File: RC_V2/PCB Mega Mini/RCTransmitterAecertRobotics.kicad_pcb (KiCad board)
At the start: 2 copper layers, 124.5 x 86.4 mm, 39 parts, among them K1 KCD1 Power Switch

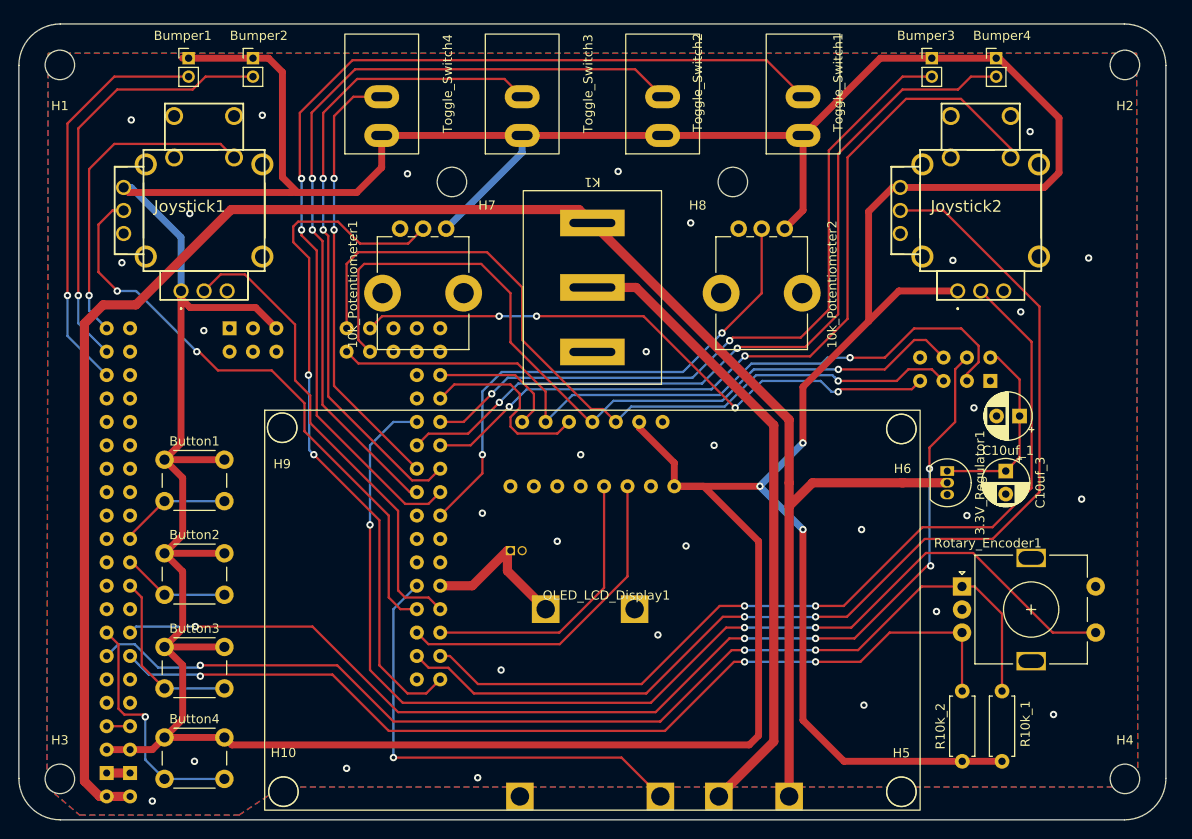
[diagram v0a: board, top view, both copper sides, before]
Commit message: rcv2 pcb finished, added new gait
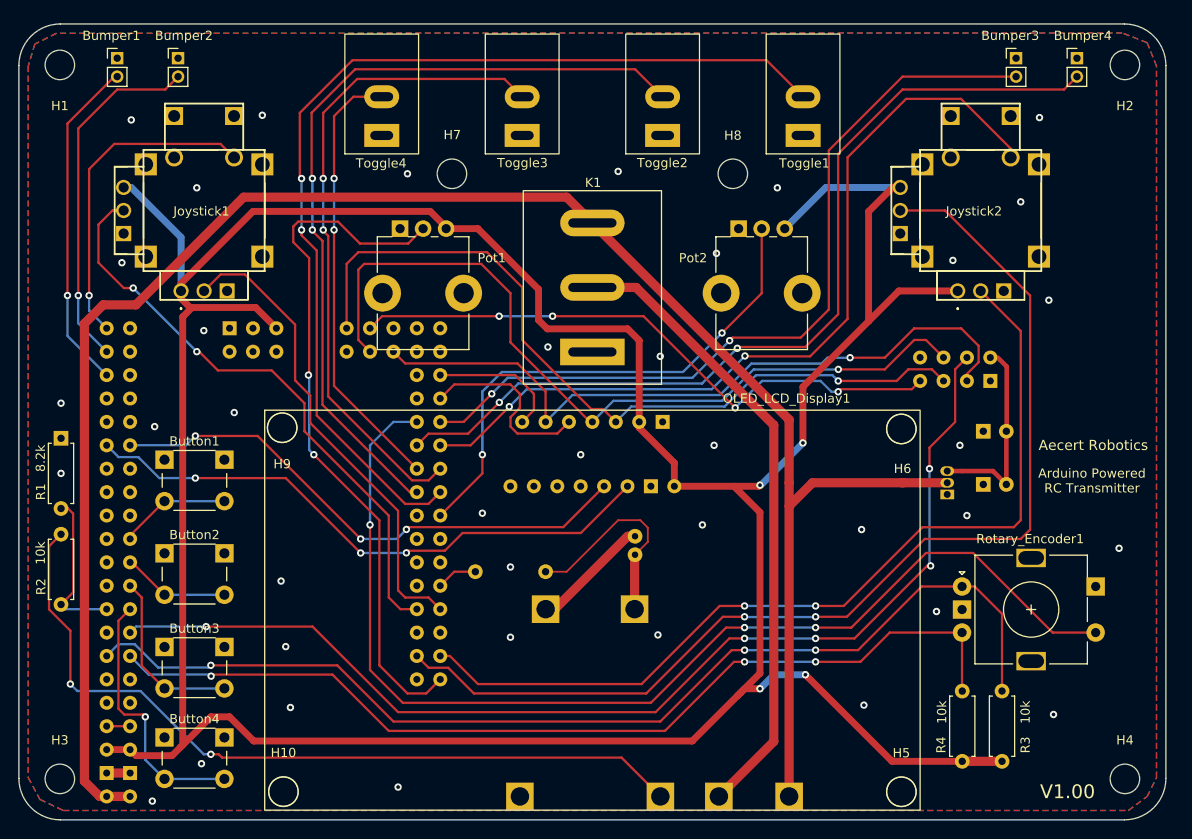
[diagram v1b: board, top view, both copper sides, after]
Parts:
- added G***: LOGO, LOGO, F.Cu at (195.8, 91.4)
- added R1: 8.2k, Resistor_THT:R_Axial_DIN0207_L6.3mm_D2.5mm_P7.62mm_Horizontal, F.Cu at (83.3, 100.8)
- added R2: 10k, Resistor_THT:R_Axial_DIN0207_L6.3mm_D2.5mm_P7.62mm_Horizontal, F.Cu at (83.3, 118.9)
- added R5: 10k, Resistor_THT:R_Axial_DIN0207_L6.3mm_D2.5mm_P7.62mm_Horizontal, B.Cu at (135.9, 115.3)
- 3.3V_Reg1: renamed from 3.3V_Regulator1; moved to B.Cu
- Arduino_Mega_Pro1: renamed from M1; value ~ -> Arduino Mega Pro Mini
- C1: renamed from C10uf_1; moved to B.Cu
- C2: renamed from C10uf_3; moved to B.Cu
- JST_Connector1: footprint Connector_PinSocket_1.27mm:PinSocket_1x02_P1.27mm_Vertical -> AddedFootprints:JST Female Connector
- Pot1: renamed from 10k_Potentiometer1; value PTV09A-4220F-B103 -> 10k
- Pot2: renamed from 10k_Potentiometer2; value PTV09A-4220F-B103 -> 10k
- R3: renamed from R10k_1; value R 10k -> 10k
- R4: renamed from R10k_2; value R 10k -> 10k
- moved JST_Connector1 14.8 mm to (145.6, 107.1), turned to 0 degrees
- moved Bumper3 9.14 mm to (186.9, 59.6)
- moved Bumper4 8.76 mm to (193.5, 59.6)
- moved Bumper2 8.13 mm to (96.0, 59.6)
- moved Bumper1 7.75 mm to (89.4, 59.6)
- moved C1 2.19 mm to (185.9, 100.1)
- moved C2 1.45 mm to (185.9, 105.8), turned to 180 degrees
- moved H7 0.89 mm to (125.7, 72.1)
- moved H8 0.89 mm to (156.2, 72.1)
- renumbered Toggle_Switch1 to Toggle1, Toggle_Switch2 to Toggle2, Toggle_Switch3 to Toggle3, Toggle_Switch4 to Toggle4
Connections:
- Arduino_Mega_Pro1 pad 20: unconnected-(M1-D20(SDA)-Pad20) -> /SDA
- Arduino_Mega_Pro1 pad 21: unconnected-(M1-D21(SCL)-Pad21) -> /SCL
- Arduino_Mega_Pro1 pad 49: unconnected-(M1-D49-Pad49) -> /CE
- Arduino_Mega_Pro1 pad 5: /Button D -> unconnected-(Arduino_Mega_Pro1-D5-Pad5)
- Arduino_Mega_Pro1 pad 53: /CE -> unconnected-(Arduino_Mega_Pro1-D53(CE)-Pad53)
- Arduino_Mega_Pro1 pad 6: unconnected-(M1-D6-Pad6) -> /Button D
- Arduino_Mega_Pro1 pad 7: unconnected-(M1-D7-Pad7) -> /Charging
- Arduino_Mega_Pro1 pad A4: /SDA -> unconnected-(Arduino_Mega_Pro1-PadA4)
- Arduino_Mega_Pro1 pad A5: /SCL -> unconnected-(Arduino_Mega_Pro1-PadA5)
- Arduino_Mega_Pro1 pad A8: /Bat+ -> /Battery Voltage
- Arduino_Mega_Pro1 pad A9: /In+ -> unconnected-(Arduino_Mega_Pro1-PadA9)
- Battery_Charger1 pad 3: /In+ -> Net-(Battery_Charger1-IN+)
- Bumper1 pad 1: /5v -> GND
- Bumper2 pad 1: /5v -> GND
- Bumper3 pad 1: /5v -> GND
- Bumper4 pad 1: /5v -> GND
- Button1 pad 1: /5v -> GND
- Button2 pad 1: /5v -> GND
- Button3 pad 1: /5v -> GND
- Button4 pad 1: /5v -> GND
- Joystick1 pad D1: unconnected-(Joystick1-NO_2-PadD1) -> GND
- Joystick1 pad MH1: unconnected-(Joystick1-PadMH1) -> GND
- Joystick1 pad MH2: unconnected-(Joystick1-PadMH2) -> GND
- Joystick1 pad MH3: unconnected-(Joystick1-PadMH3) -> GND
- Joystick1 pad MH4: unconnected-(Joystick1-PadMH4) -> GND
- Joystick2 pad D1: unconnected-(Joystick2-NO_2-PadD1) -> GND
- Joystick2 pad MH1: unconnected-(Joystick2-PadMH1) -> GND
- Joystick2 pad MH2: unconnected-(Joystick2-PadMH2) -> GND
- Joystick2 pad MH3: unconnected-(Joystick2-PadMH3) -> GND
- Joystick2 pad MH4: unconnected-(Joystick2-PadMH4) -> GND
- Toggle1 pad 1: /5v -> GND
- Toggle2 pad 1: /5v -> GND
- Toggle3 pad 1: /5v -> GND
- Toggle4 pad 1: /5v -> GND
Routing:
- net /5v: track 510.3 -> 361.0 mm, vias 3 -> 4
- net Net-(Battery_Charger1-IN+): track 0.00 -> 86.8 mm, vias 0 -> 2
- net /In+: track 50.4 -> 0.00 mm, vias 1 -> 0
- net /SCL: track 36.2 -> 64.4 mm, vias 0 -> 3
- net /SDA: track 30.8 -> 58.9 mm, vias 0 -> 3
- net /Charging: track 0.00 -> 17.1 mm
- net /Bat-: track 0.00 -> 13.0 mm
- net /Right Bumper A: track 79.0 -> 88.1 mm
- net /Right Bumper B: track 89.6 -> 98.4 mm
- net /Left Bumper B: track 46.8 -> 38.7 mm
- net /Left Bumper A: track 44.3 -> 36.6 mm
- net /Bat+: track 16.9 -> 23.2 mm
- net /CE: track 83.0 -> 77.9 mm
- net /Battery Voltage: track 0.00 -> 4.44 mm
- net /Button D: track 26.2 -> 28.7 mm
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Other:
- board text added: "+"
- board text added: "-"
- board text added: "Aecert Robotics"
- board text added: "Arduino Powered RC Transmitter"
- board text added: "V1.00"

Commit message: Fixed pin placement and hole diameter
after testing in real life, i made some changes
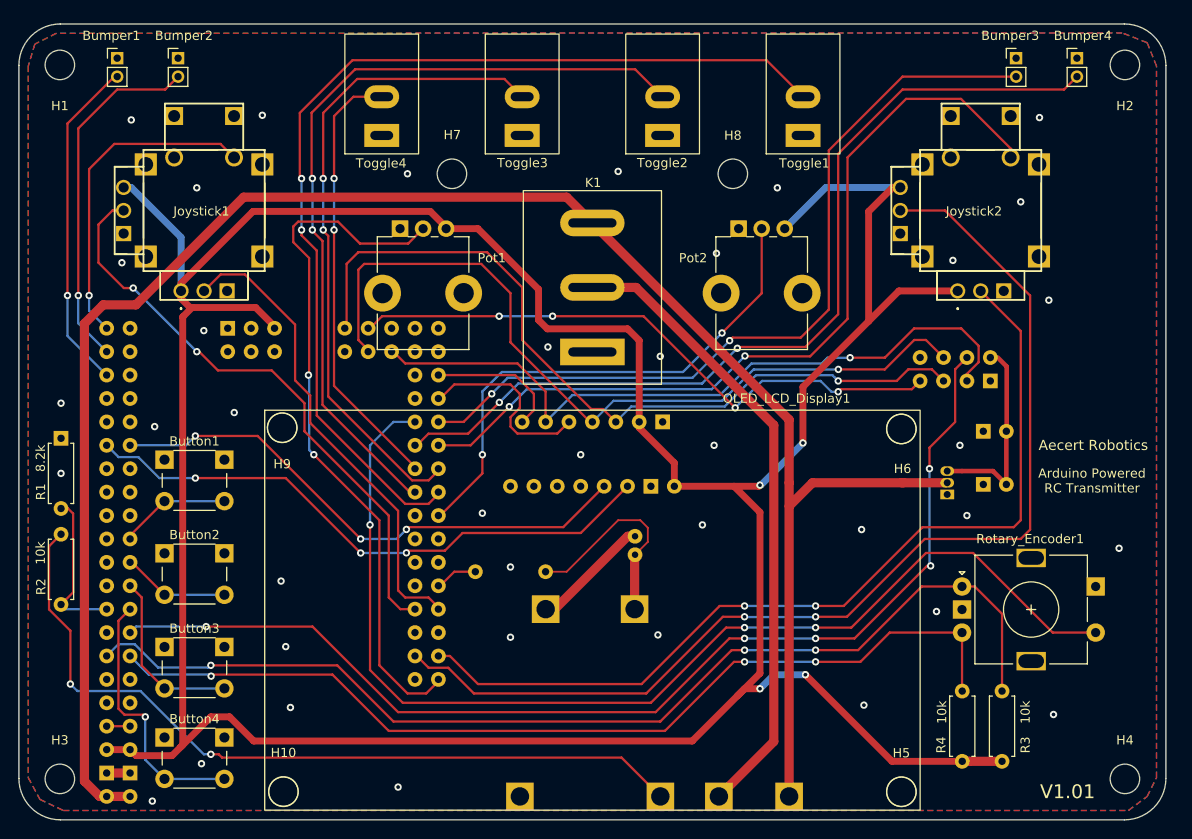
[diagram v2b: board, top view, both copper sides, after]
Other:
- board text added: "V1.01"
- board text removed: "V1.00"

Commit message: updated code pins and pcb
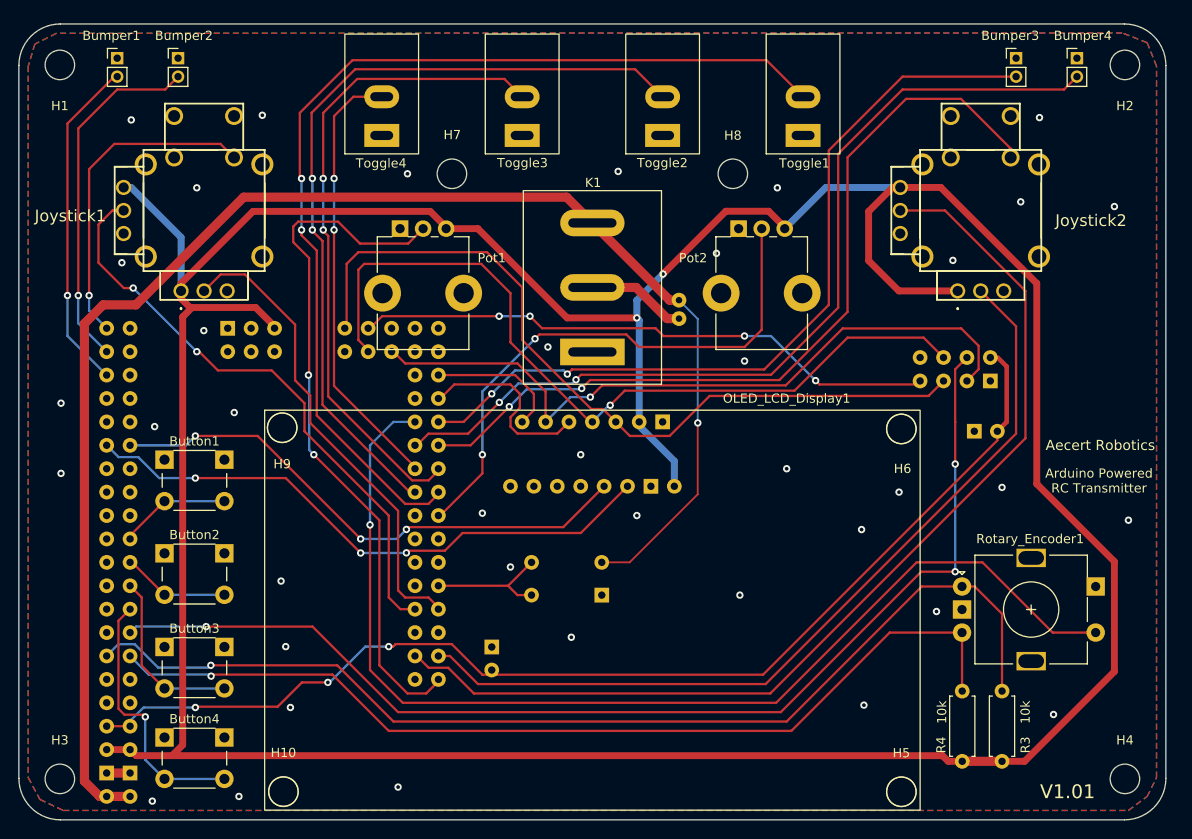
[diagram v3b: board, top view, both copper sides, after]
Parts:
- removed 3.3V_Reg1: HT7333-3.3_TO92, Package_TO_SOT_THT:TO-92_Inline
- removed Battery_Charger1: J5019 Charger, AddedFootprints:J5019 Charger
- removed R5: 10k, Resistor_THT:R_Axial_DIN0207_L6.3mm_D2.5mm_P7.62mm_Horizontal
- R1: value 8.2k -> 10k; moved to B.Cu
- R2: moved to B.Cu
- moved C2 59.4 mm to (130.0, 126.0), turned to 90 degrees
- moved R2 58.7 mm to (142.0, 117.9), turned to 180 degrees
- moved R1 52.8 mm to (134.4, 114.3), turned to 0 degrees
- moved JST_Connector1 15.7 mm to (150.4, 92.2), turned to 180 degrees
- moved C1 0.98 mm to (184.9, 100.1)
- moved G*** 0.76 mm to (196.5, 91.4)
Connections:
- Arduino_Mega_Pro1 pad 7: /Charging -> unconnected-(Arduino_Mega_Pro1-D7-Pad7)
- Arduino_Mega_Pro1 pad VIN: /Vin -> /Bat+
- C1 pad 1: Net-(3.3V_Reg1-VO) -> /3.3v
- C2 pad 1: Net-(3.3V_Reg1-VO) -> /3.3v
- Joystick1 pad MH1: GND -> unconnected-(Joystick1-PadMH1)
- Joystick1 pad MH2: GND -> unconnected-(Joystick1-PadMH2)
- Joystick1 pad MH3: GND -> unconnected-(Joystick1-PadMH3)
- Joystick1 pad MH4: GND -> unconnected-(Joystick1-PadMH4)
- Joystick2 pad MH1: GND -> unconnected-(Joystick2-PadMH1)
- Joystick2 pad MH2: GND -> unconnected-(Joystick2-PadMH2)
- Joystick2 pad MH3: GND -> unconnected-(Joystick2-PadMH3)
- Joystick2 pad MH4: GND -> unconnected-(Joystick2-PadMH4)
- K1 pad 2: /VOUT- -> /Bat-
- K1 pad 3: /Vin -> /Bat+
- NRF24 pad 1: Net-(3.3V_Reg1-VO) -> /3.3v
- R1 pad 1: GND -> /Battery Voltage
- R1 pad 2: /Charging -> /Bat+
- R2 pad 1: /Charging -> GND
- R2 pad 2: Net-(Battery_Charger1-IN+) -> /Battery Voltage
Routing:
- net /Vin: track 201.8 -> 0.00 mm
- net /Bat+: track 23.2 -> 165.5 mm, vias 0 -> 1
- net /3.3v: track 2.54 -> 123.6 mm, vias 0 -> 3
- net Net-(Battery_Charger1-IN+): track 86.8 -> 0.00 mm, vias 2 -> 0
- net /VOUT-: track 68.6 -> 0.00 mm
- net /5v: track 361.0 -> 391.6 mm, vias 4 -> 2
- net Net-(3.3V_Reg1-VO): track 22.0 -> 0.00 mm
- net /Charging: track 17.1 -> 0.00 mm
- net /Battery Voltage: track 4.44 -> 14.1 mm
- net /Joy Right Y: track 118.9 -> 112.4 mm, vias 2 -> 0
- net /Joy Right X: track 98.3 -> 92.1 mm, vias 2 -> 0
- net /Pot Right: track 57.1 -> 60.5 mm
- net /MISO: track 66.5 -> 63.5 mm
- net /Bat-: track 13.0 -> 10.8 mm
- net /NRF CSN: track 121.9 -> 123.7 mm, vias 5 -> 3
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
